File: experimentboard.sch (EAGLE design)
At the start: 183 parts, among them IC1 TL072P, IC2 LM317, IC3 LM337, IC4 TL072P, IC5 TL072P, IC6 TL072P, P1 PLR135/T9, P9 P9, Q1 BS170, Q2 BS170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

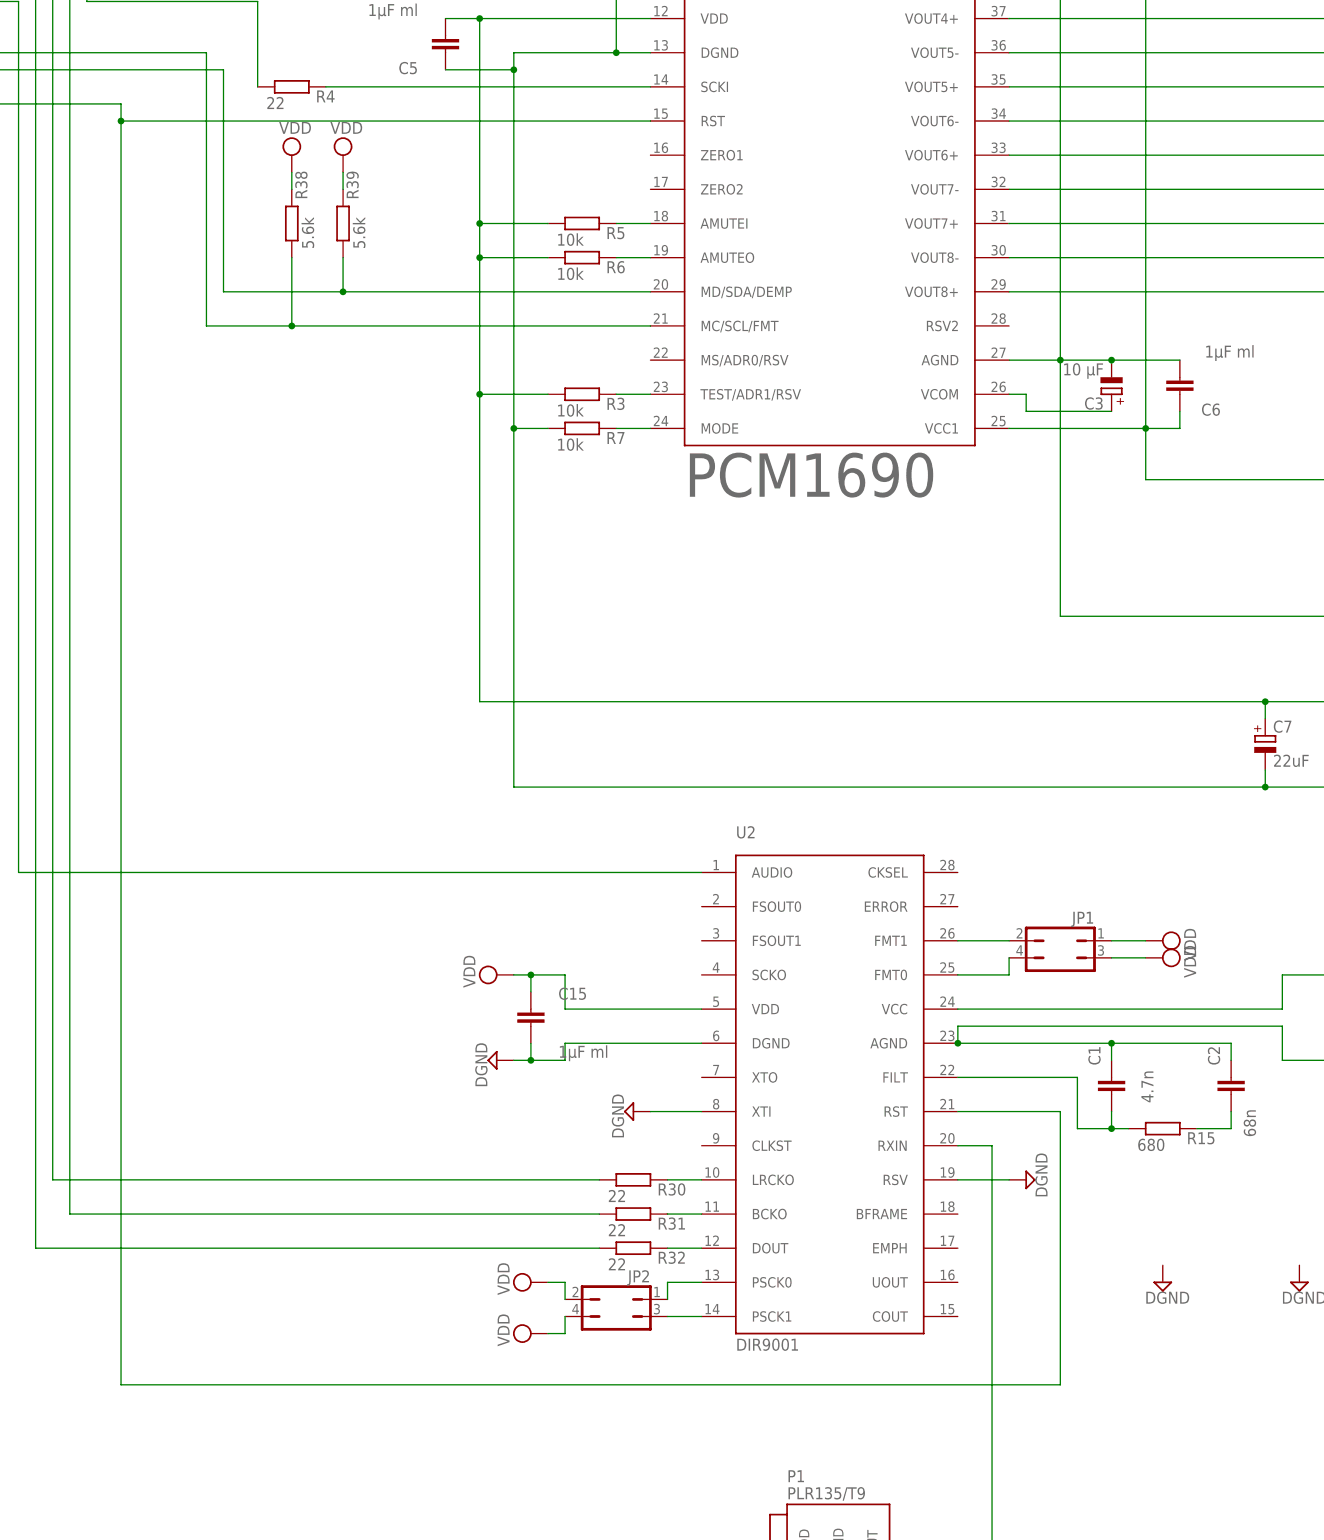
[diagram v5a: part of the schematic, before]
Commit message: Jumper info on silkscreen
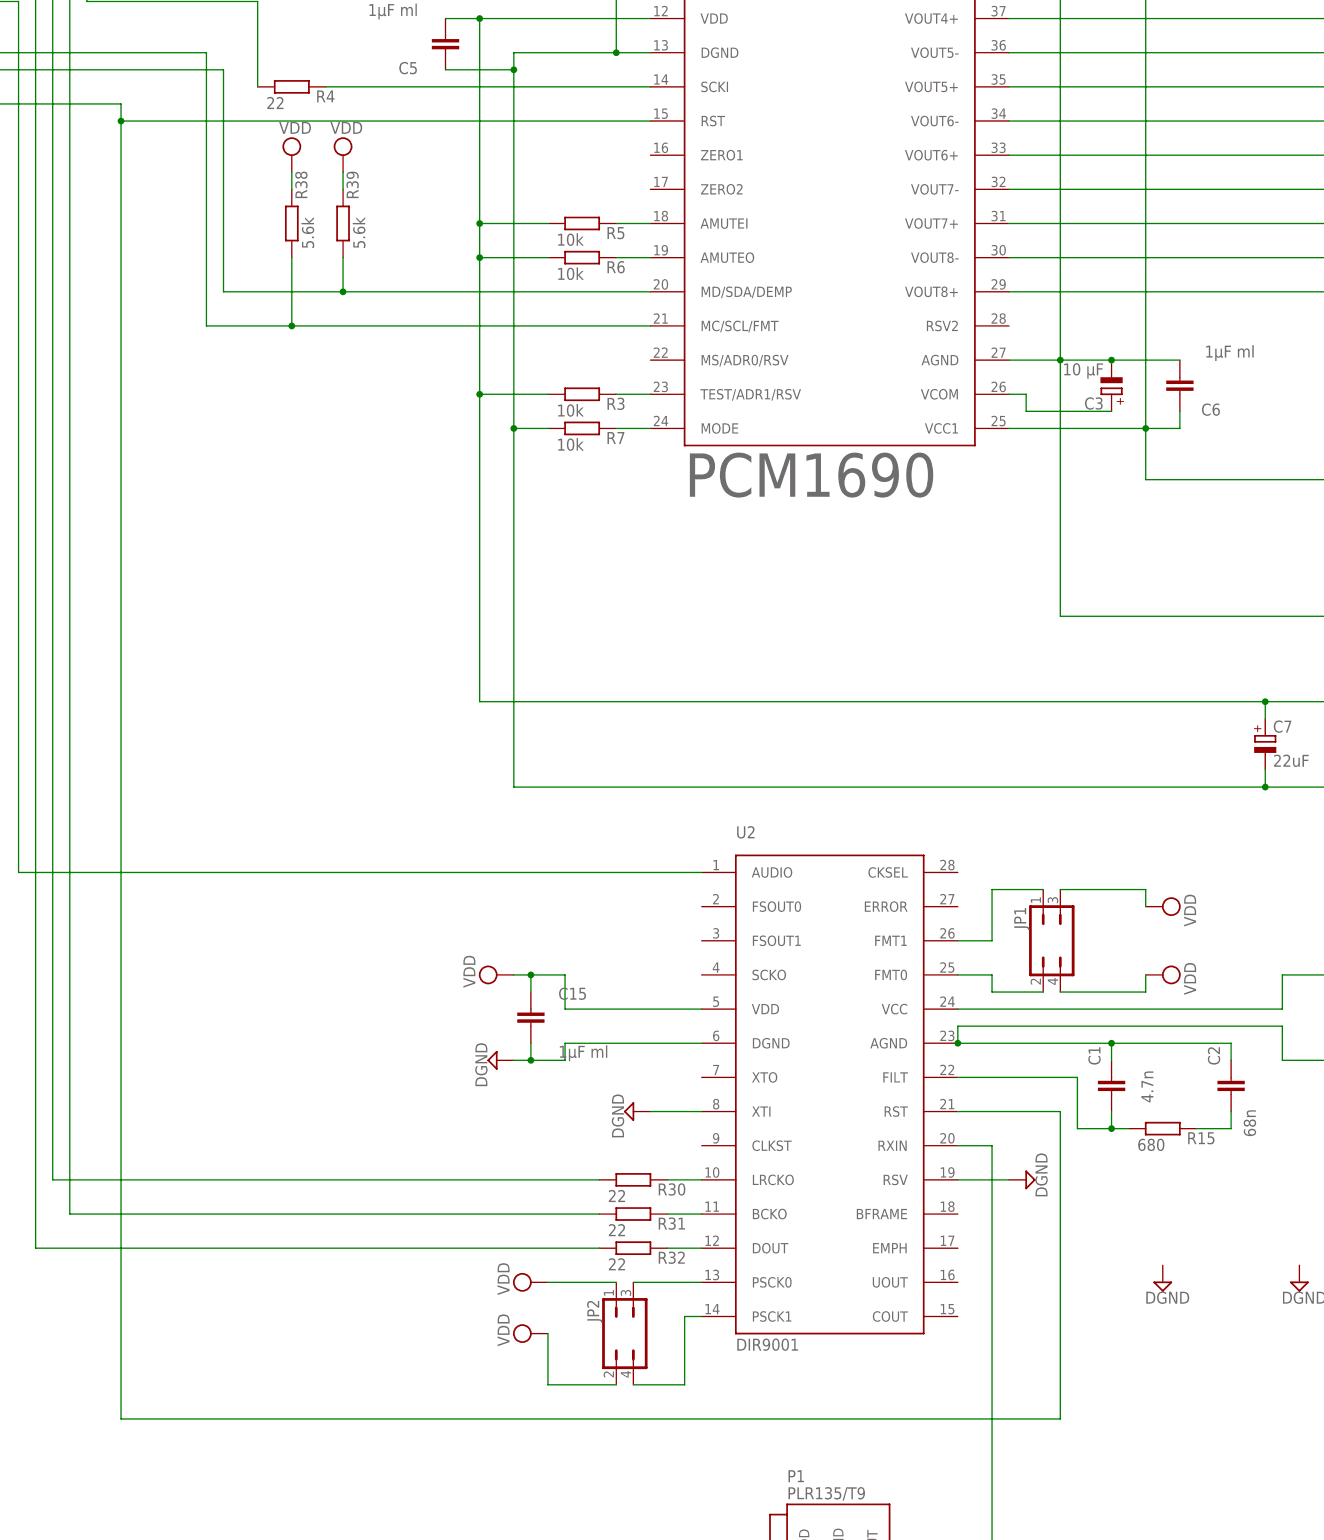
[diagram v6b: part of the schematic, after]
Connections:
- net N$1: now also JP2.4; no longer JP2.3
- net N$3: now also JP2.3; no longer JP2.1
- net N$7: now also JP1.2; no longer JP1.4
- net N$8: now also JP1.1; no longer JP1.2
- net VDD: now also JP1.4, JP2.1; no longer JP1.1, JP2.4
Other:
- moved on the sheet: JP1, JP2

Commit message: SCKO selection jumper removed: unneeded
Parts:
- removed JP4: (no value), jumper:JP1Q
- JP2: device jumper:JP2Q -> jumper:JP1Q
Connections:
- removed net N$1: JP2.4, U2.PSCK1
- removed net N$3: JP2.3, U2.PSCK0
- net AGND: now also JP3.2; no longer JP4.2
- net DGND: now also JP3.1; no longer JP4.1
- net VCC: now also JP2.2; no longer JP3.2
- net VDD: no longer JP2.1, JP2.2
- net VDD_5V: now also JP2.1; no longer JP3.1
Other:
- moved on the sheet: JP3
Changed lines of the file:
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@@
 <part name="SUPPLY20" library="supply2" deviceset="VDD" device=""/>
 <part name="SUPPLY25" library="supply2" deviceset="VDD" device=""/>
-<part name="JP2" library="jumper" deviceset="JP2Q" device=""/>
-<part name="SUPPLY24" library="supply2" deviceset="VDD" device=""/>
-<part name="SUPPLY26" library="supply2" deviceset="VDD" device=""/>
 <part name="SUPPLY17" library="supply2" deviceset="DGND" device=""/>
 <part name="SUPPLY18" library="supply2" deviceset="DGND" device=""/>
@@
 <part name="C13" library="rcl" deviceset="CPOL-EU" device="E2.5-6" value="100uF/25V"/>
 <part name="C14" library="rcl" deviceset="CPOL-EU" device="E2.5-6" value="100uF/25V"/>
+<part name="JP2" library="jumper" deviceset="JP1Q" device=""/>
+<part name="C16" library="rcl" deviceset="CPOL-EU" device="E2-5" value="10 µF"/>
 <part name="JP3" library="jumper" deviceset="JP1Q" device=""/>
-<part name="C16" library="rcl" deviceset="CPOL-EU" device="E2-5" value="10 µF"/>
-<part name="JP4" library="jumper" deviceset="JP1Q" device=""/>
 <part name="SUPPLY4" library="supply2" deviceset="VDD" device=""/>
 <part name="SUPPLY10" library="supply2" deviceset="DGND" device=""/>
@@
 <instance part="SUPPLY20" gate="G$1" x="152.4" y="-68.58" rot="R270"/>
 <instance part="SUPPLY25" gate="G$1" x="152.4" y="-78.74" rot="R270"/>
-<instance part="JP2" gate="B1" x="71.12" y="-132.08" rot="MR180"/>
-<instance part="SUPPLY24" gate="G$1" x="58.42" y="-124.46" rot="R90"/>
-<instance part="SUPPLY26" gate="G$1" x="58.42" y="-132.08" rot="R90"/>
 <instance part="SUPPLY17" gate="G$1" x="73.66" y="-99.06" rot="R270"/>
 <instance part="SUPPLY18" gate="G$1" x="132.08" y="-109.22" rot="R90"/>
@@
 <instance part="C13" gate="G$1" x="177.8" y="215.9"/>
 <instance part="C14" gate="G$1" x="185.42" y="215.9"/>
-<instance part="JP3" gate="A" x="-99.06" y="83.82" rot="R90"/>
+<instance part="JP2" gate="A" x="-99.06" y="83.82" rot="R90"/>
 <instance part="C16" gate="G$1" x="96.52" y="-187.96" rot="R90"/>
-<instance part="JP4" gate="A" x="124.46" y="215.9" rot="R90"/>
+<instance part="JP3" gate="A" x="124.46" y="215.9" rot="R90"/>
 <instance part="SUPPLY4" gate="G$1" x="193.04" y="-78.74" rot="R270"/>
 <instance part="SUPPLY10" gate="G$1" x="195.58" y="-91.44" rot="R90"/>
@@
 <pinref part="JP1" gate="B1" pin="3"/>
 <wire x1="149.86" y1="-66.04" x2="137.16" y2="-66.04" width="0.1524" layer="91"/>
-</segment>
-<segment>
-<pinref part="SUPPLY24" gate="G$1" pin="VDD"/>
-<pinref part="JP2" gate="B1" pin="1"/>
-<wire x1="60.96" y1="-124.46" x2="71.12" y2="-124.46" width="0.1524" layer="91"/>
-</segment>
-<segment>
-<pinref part="JP2" gate="B1" pin="2"/>
-<pinref part="SUPPLY26" gate="G$1" pin="VDD"/>
-<wire x1="71.12" y1="-139.7" x2="60.96" y2="-139.7" width="0.1524" layer="91"/>
-<wire x1="60.96" y1="-139.7" x2="60.96" y2="-132.08" width="0.1524" layer="91"/>
 </segment>
 </net>
@@
 <pinref part="SUPPLY13" gate="G$1" pin="DGND"/>
 <wire x1="132.08" y1="215.9" x2="132.08" y2="213.36" width="0.1524" layer="91"/>
-<pinref part="JP4" gate="A" pin="1"/>
+<pinref part="JP3" gate="A" pin="1"/>
 </segment>
 <segment>
@@
 <wire x1="55.88" y1="223.52" x2="55.88" y2="215.9" width="0.1524" layer="91"/>
 <pinref part="SUPPLY16" gate="G$1" pin="AGND"/>
-<pinref part="JP4" gate="A" pin="2"/>
+<pinref part="JP3" gate="A" pin="2"/>
 <wire x1="116.84" y1="215.9" x2="114.3" y2="215.9" width="0.1524" layer="91"/>
 <junction x="114.3" y="215.9"/>
@@
 <pinref part="SUPPLY28" gate="G$1" pin="VCC"/>
 <wire x1="-109.22" y1="83.82" x2="-109.22" y2="91.44" width="0.1524" layer="91"/>
-<pinref part="JP3" gate="A" pin="2"/>
+<pinref part="JP2" gate="A" pin="2"/>
 <wire x1="-106.68" y1="83.82" x2="-109.22" y2="83.82" width="0.1524" layer="91"/>
 </segment>
@@
 <segment>
 <pinref part="P9" gate="G$1" pin="VDD_5V"/>
-<pinref part="JP3" gate="A" pin="1"/>
+<pinref part="JP2" gate="A" pin="1"/>
 <wire x1="-86.36" y1="83.82" x2="-91.44" y2="83.82" width="0.1524" layer="91"/>
 </segment>
@@
 </segment>
 </net>
-<net name="N$1" class="0">
-<segment>
-<pinref part="U2" gate="G$1" pin="PSCK1"/>
-<wire x1="83.82" y1="-129.54" x2="81.28" y2="-129.54" width="0.1524" layer="91"/>
-<wire x1="81.28" y1="-129.54" x2="81.28" y2="-139.7" width="0.1524" layer="91"/>
-<pinref part="JP2" gate="B1" pin="4"/>
-<wire x1="81.28" y1="-139.7" x2="73.66" y2="-139.7" width="0.1524" layer="91"/>
-</segment>
-</net>
-<net name="N$3" class="0">
-<segment>
-<pinref part="U2" gate="G$1" pin="PSCK0"/>
-<pinref part="JP2" gate="B1" pin="3"/>
-<wire x1="83.82" y1="-124.46" x2="73.66" y2="-124.46" width="0.1524" layer="91"/>
-</segment>
-</net>
